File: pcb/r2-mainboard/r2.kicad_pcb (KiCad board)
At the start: 4 copper layers, 185.5 x 95 mm, 327 parts, among them J1 USB-C 16P, J2 Pico-Lock 504050-0391, J20 SWD+JTAG (DNP), J21 MICRO_SD(TFC-WPAPR-08), J22 HC-FPC-05-09-6RLTAG, J23 HC-FPC-05-09-6RLTAG, J24 HC-FPC-05-09-8RLTAG, J25 SolderPads 3x, J26 BTH-060-01-L-D-A-K-TR, J27 BTH-060-01-L-D-A-K-TR, J6 FPC-05F-50PH20, Q1 AO3401A, Q2 S8050, Q6 AO3400A, Q7 AO3401A, Q8 AO3401A, Q9 AO3400A, SW20 SW, SW21 SW, SW22 SW, U1 BQ25892RTW, U10 TPS7A0233DBVR, U12 TPS61022RWUR, U13 TPS63802DLAR, U14 TPS62A02DRLR, U15 TPS62A02DRLR, U2 MAX17048G+T10, U20 STM32G0B1RCT6, U21 INA3221, U22 INA3221, U23 LGS6302B5, U24 LGS6302B5, U26 LGS5145, U27 INA3221, U3 USBLC6-2SC6, U31 LM321, U41 XC6SLX-FTG256, U42 W25Q128JVSIQ, U52 MT41K64M16TW, U53 LM3630A, U54 TPS22914BYFPR, U55 TPS22914BYFPR, U6 MT9700, U7 TPS22914BYFPR, U8 TPS22914BYFPR, U9 LGS5145, X1 33.33MHz, X2 PCM-071, Y20 32.768kHz

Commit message: R2: settings applied, and 200 of the board's 244 DRC errors were mine
The owner ran tools/import_r1_settings.py --write. check_pcb.py now reports
8 of 8 net classes present, 122 nets assigned, 0 dead patterns.

Their own KiCad "import settings from another project" had already pulled R1's
constraints and presets across first, which is visible in the script's before
column -- and shows exactly why that is not enough on its own: it brought R1's
class NAMES (DP, LVDS, SDRAM_A/H/L, POWER) and R1's patterns, none of which
match an R2 net. Every net would have routed on Default.

Then the DRC that followed found 244 violations, 200 of them solder_mask_bridge
on J26 and J27 -- footprints this repo generates. They are not a mistake:
MASK_MARGIN 0.102 on a 0.5 mm pitch makes each aperture 0.509, so a row is one
gang opening, which is what Samtec's own footprint does and what the pitch
requires (the 0.093 web the alternative needs is under JLCPCB's 0.1 minimum and
would be dropped anyway, silently). What was missing is the attribute that tells
KiCad so. Both footprints, the generator, and the two placed instances now carry
`allow_soldermask_bridges`. Board total: 244 -> 44, and the 44 left are silk and
edge-clearance noise that placement will clear.

Samtec's file lacks the attribute only because it is a tedit-era KiCad 5/6
footprint that predates it.

Two things learned, both recorded:

- `kicad-cli pcb drc` SILENTLY IGNORES a .kicad_dru it cannot parse. No error,
  no warning, exit 0, rules just not applied -- verified by feeding it a
  deliberately unterminated rule and getting identical clean output. So the
  clean run on r2.kicad_dru proves nothing about its validity; only Board Setup
  > Custom Rules > "Check rule syntax" does. layout.md §9.2, and the script now
  says so on exit.

- Patching footprints in a loop over re.finditer while mutating the text skips
  every match after the first, because the offsets shift. J26 was silently left
  unpatched and only surfaced as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
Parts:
- moved C1 10.5 mm to (57.0, 37.0)
- moved C2 10.4 mm to (61.0, 35.5), turned to 180 degrees
- moved L1 2.60 mm to (68.0, 36.0)
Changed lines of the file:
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@@
 		(35 "F.Fab" user)
 		(33 "B.Fab" user)
-		(39 "User.1" user)
-		(41 "User.2" user)
-		(43 "User.3" user)
-		(45 "User.4" user)
 	)
 	(setup
@@
 		(capping no)
 		(filling no)
+		(zone_defaults)
 		(pcbplotparams
 			(layerselection 0x00000000_00000000_55555555_5755f5ff)
@@
 			)
 		)
-		(attr smd)
+		(attr smd allow_soldermask_bridges)
 		(duplicate_pad_numbers_are_jumpers no)
 		(fp_line
@@
 	(footprint "Capacitor_SMD:C_0402_1005Metric"
 		(layer "F.Cu")
-		(at 50.81 45.53)
+		(at 57 37)
 		(descr "Capacitor SMD 0402 (1005 Metric), square (rectangular) end terminal, IPC-7351 nominal, (Body size source: IPC-SM-782 page 76, https://www.pcb-3d.com/wordpress/wp-content/uploads/ipc-sm-782a_amendment_1_and_2.pdf)")
 		(tags "capacitor")
@@
 	(footprint "Inductor_SMD:L_Taiyo-Yuden_NR-30xx"
 		(layer "F.Cu")
-		(at 65.6 37)
+		(at 68 36)
 		(descr "Inductor, Taiyo Yuden, NR series, Taiyo-Yuden_NR-30xx, 3.0mmx3.0mm")
 		(tags "inductor taiyo-yuden nr smd")
@@
 			)
 		)
-		(attr smd)
+		(attr smd allow_soldermask_bridges)
 		(duplicate_pad_numbers_are_jumpers no)
 		(fp_line
@@
 	(footprint "Capacitor_SMD:C_0805_2012Metric"
 		(layer "F.Cu")
-		(at 51.6 31)
+		(at 61 35.5 180)
 		(descr "Capacitor SMD 0805 (2012 Metric), square (rectangular) end terminal, IPC-7351 nominal, (Body size source: IPC-SM-782 page 76, https://www.pcb-3d.com/wordpress/wp-content/uploads/ipc-sm-782a_amendment_1_and_2.pdf, https://docs.google.com/spreadsheets/d/1BsfQQcO9C6DZCsRaXUlFlo91Tg2WpOkGARC1WS5S8t0/edit?usp=sharing)")
 		(tags "capacitor")
 		(property "Reference" "C2"
-			(at 0 -1.68 0)
+			(at -2.5 3 0)
 			(layer "F.SilkS")
 			(effects
@@
 		(duplicate_pad_numbers_are_jumpers no)
 		(fp_line
-			(start -0.261252 -0.735)
-			(end 0.261252 -0.735)
+			(start -0.261252 0.735)
+			(end 0.261252 0.735)
 			(stroke
 				(width 0.12)
@@
 		)
 		(fp_line
-			(start -0.261252 0.735)
-			(end 0.261252 0.735)
+			(start -0.261252 -0.735)
+			(end 0.261252 -0.735)
 			(stroke
 				(width 0.12)
@@
 		)
 		(fp_text user "${REFERENCE}"
-			(at 0 0 0)
+			(at 0 0 180)
 			(unlocked yes)
 			(layer "F.Fab")
@@
 		)
 		(pad "1" smd roundrect
-			(at -0.95 0)
+			(at -0.95 0 180)
 			(size 1 1.45)
 			(layers "F.Cu" "F.Mask" "F.Paste")
@@
 		)
 		(pad "2" smd roundrect
-			(at 0.95 0)
+			(at 0.95 0 180)
 			(size 1 1.45)
 			(layers "F.Cu" "F.Mask" "F.Paste")
@@
 		(tags "WQFN NoLead")
 		(property "Reference" "U1"
-			(at 0 -3.33 0)
+			(at 4.05 -1.85 0)
 			(layer "F.SilkS")
 			(effects
@@
 		(layer "Edge.Cuts")
 	)
+	(segment
+		(start 60.45 39.35)
+		(end 60.5 39.3)
+		(width 0.1)
+		(layer "F.Cu")
+		(net "GND")
+	)
+	(segment
+		(start 60.5 39.3)
+		(end 60.5 39)
+		(width 0.1)
+		(layer "F.Cu")
+		(net "GND")
+	)
 	(group "SoM: X2 + J26 + J27"

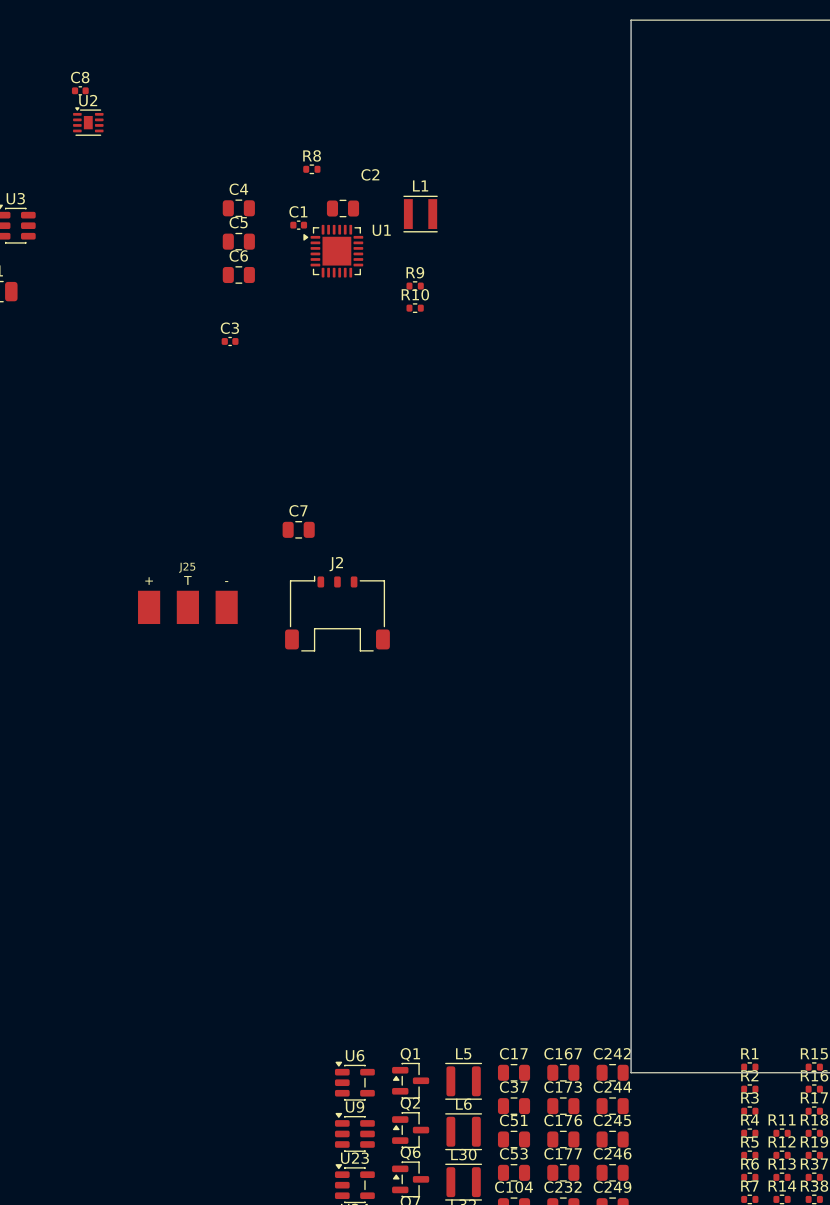
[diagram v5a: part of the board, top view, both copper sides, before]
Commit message: R2: C6 goes 0805/10V -> 0603/16V, and clears two DRC errors doing it
The question was whether the REGN decoupling cap could be smaller. It can,
and the smaller part is the better part -- but not for the reason the doc
gave.

bq25896.pdf pin 22 asks for "a 4.7 uF (10 V rating) ceramic capacitor",
placed close to the IC, and gives no range around it -- unlike tps63802.pdf
which publishes a 10-50 uF window for its output cap. So the value is fixed
and the package is the only free variable. REGN sits at 4.7-4.8 V here (spec
table, V(VBUS) = 5 V), and a ceramic loses capacitance with the field across
its dielectric, so a higher rating in a smaller case can beat a lower rating
in a larger one.

Fitted: LCSC C19666, Samsung CL10A475KO8NNNC, 4.7 uF 16 V X5R 0603, a JLCPCB
basic part with 6.35 M in stock. It keeps TI's value, exceeds TI's rating,
and is smaller and lower-ESL than the 0805 -- which serves bq25896.pdf
section 12.1 guideline 6 better than the part it replaces. 0402 was rejected:
the cheap one is +-20 % before derating at 2.1x voltage margin, and the 25 V
one costs 4x a basic part to save 0.7 mm2.

DRC went 46 -> 44. The 0805's pad 2 sat 0.075 mm from a Net-(C3-Pad2) track
against the PWR netclass's 0.110 mm; 0603 pulls it back 0.175 mm and clears
both violations. Unconnected unchanged at 499, ERC unchanged at 32.

battery.md section 6 is corrected while here. It claimed the TS divider's
loading is why 4.7 uF is not optional. It is not -- that divider draws 377 uA
of steady DC, which constrains the LDO, not the capacitor. The reasons are
pin 22 and the gate drive. Ripple was checked and is not binding either: even
at a generous 20 nC per cycle, 1 uF effective gives 0.42 % of REGN against
1-1.4 % TS hysteresis bands.

C6 also gained the check_pcb.py proximity rule it never had, 5.0 mm to U1,
the same limit as its neighbours C1/C2/C3. It sits at 4.15 mm and passes.

Note: r2.kicad_pcb and r2.kicad_pro in this commit also carry the owner's
uncommitted placement wor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
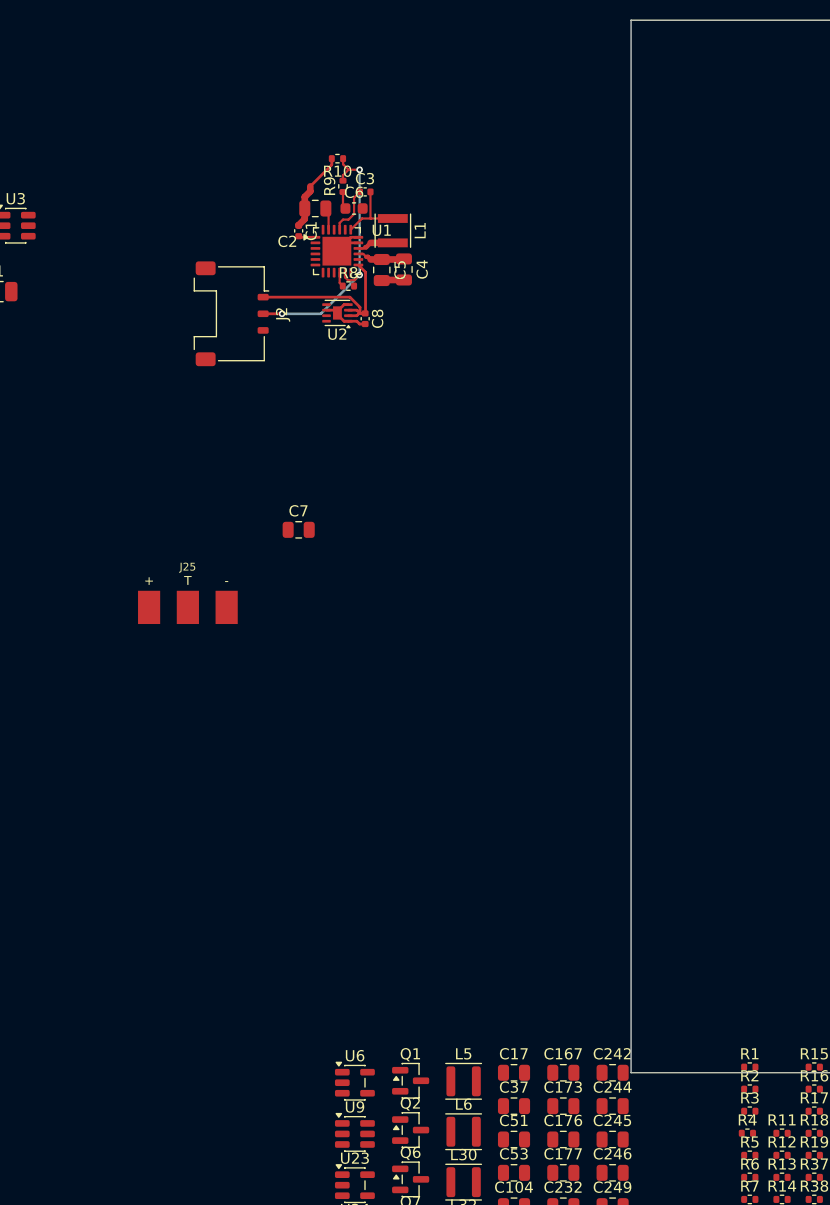
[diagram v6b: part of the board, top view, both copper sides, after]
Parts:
- C6: value 4.7uF/10V -> 4.7uF/16V; footprint Capacitor_SMD:C_0805_2012Metric -> Capacitor_SMD:C_0603_1608Metric
- moved C8 32.9 mm to (63.0, 45.4), turned to -90 degrees
- moved J2 28.6 mm to (51.0, 45.0), turned to -90 degrees
- moved U2 28.3 mm to (60.5, 44.9), turned to 180 degrees
- moved C3 18.2 mm to (63.0, 34.0)
- moved C4 15.9 mm to (66.5, 41.0), turned to -90 degrees
- moved R10 15.2 mm to (60.5, 31.0), turned to 180 degrees
- moved C5 13.2 mm to (64.5, 41.0), turned to -90 degrees
- moved C6 12.0 mm to (62.0, 35.5)
- moved R9 11.1 mm to (61.0, 33.5), turned to 90 degrees
- moved R8 11.0 mm to (61.5, 42.5)
- moved L1 2.92 mm to (65.5, 37.5), turned to -90 degrees
- moved C2 2.50 mm to (58.5, 35.5), turned to 0 degrees
- moved C1 0.52 mm to (57.0, 37.5), turned to -90 degrees
- moved R4 0.22 mm to (97.5, 119.0)
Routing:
- net /battery/CHG_TS: track 0.00 -> 25.1 mm, vias 0 -> 3
- net GND: track 0.37 -> 19.9 mm
- net +VBAT: track 0.00 -> 17.5 mm
- net +VSYS: track 0.00 -> 7.16 mm
- net Net-(C3-Pad2): track 0.00 -> 6.15 mm
- net Net-(U1-BTST): track 0.00 -> 4.46 mm
- net /battery/REGN: track 0.00 -> 1.67 mm
- net Net-(U1-PMID): track 0.00 -> 1.56 mm
- net +VBUS: track 0.00 -> 1.55 mm
- net Net-(U1-ILIM): track 0.00 -> 1.33 mm
- added copper zone on In1.Cu, net GND

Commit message: R2: withdraw the RWU0007A thermal-pad concern -- it was wrong
power.md §7 item 2 said KiCad's Texas_RWU0007A_VQFN-7_2x2mm_P0.5mm leaves the
thermal-pad segments unnumbered, so U12's heat path is not tied to GND, and to
copy the footprint into r2.pretty and renumber those pads 1 before layout.

Reading the placed footprint with the layer field visible: the six unnumbered
pads are F.Paste ONLY. They are stencil apertures -- each large pad split into
two openings to control solder volume, the standard idiom at that size. Pads
1/2/3 are F.Cu + F.Mask, numbered, and netted GND / SW / +5V_DCDC. Pin 1 is the
thermal path per Table 5-1 and it is on GND already.

Acting on the note would have renumbered paste apertures into copper and
shorted GND, SW and VOUT together -- creating the failure it was meant to
prevent. Found because the owner is routing U12 right now.

§11.2 item 5 amended to a plain layout instruction, and §8's open-items list
no longer carries it.

Co-Authored-By: Claude Opus 5 <noreply@anthropic.com>
Claude-Session: https://claude.ai/code/session_01MnesETWABbVdbcVnCKfKVs
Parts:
- removed R14, R15: 0R, Resistor_SMD:R_0402_1005Metric
- removed R16: 10k, Resistor_SMD:R_0402_1005Metric
- C4, C5, C7: footprint Capacitor_SMD:C_0805_2012Metric -> Capacitor_SMD:C_0402_1005Metric
- moved U13 139.9 mm to (75.4, 49.2)
- moved U15 127.8 mm to (77.7, 32.8)
- moved L13 126.0 mm to (77.1, 27.4)
- moved C34 125.1 mm to (83.2, 29.6)
- moved U12 123.8 mm to (101.2, 35.4)
- moved R36 122.1 mm to (81.8, 31.2)
- moved C33 121.8 mm to (76.7, 30.9)
- moved R35 120.7 mm to (79.5, 31.3)
- moved R33 120.1 mm to (80.5, 27.7)
- moved R34 120.1 mm to (80.5, 29.6)
- moved C28 120.0 mm to (101.5, 37.4)
- moved R23 119.7 mm to (101.3, 27.6)
- moved C21 118.8 mm to (79.8, 40.4), turned to -90 degrees
- moved C20 118.5 mm to (74.6, 40.4), turned to -90 degrees
- moved U10 117.2 mm to (77.2, 40.9)
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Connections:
- net /USB_DM renamed /USBD-
- net /USB_DP renamed /USBD+
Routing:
- net +VBAT: track 17.5 -> 55.8 mm
- net /battery/CHG_TS: track 25.1 -> 3.40 mm, vias 3 -> 1
- net Net-(F1-Pad1): track 0.00 -> 7.73 mm, vias 0 -> 2
- net /battery/USB_CC1: track 0.00 -> 7.44 mm
- net /battery/USB_CC2: track 0.00 -> 5.70 mm
- net Net-(J1-D--PadA7): track 0.00 -> 5.16 mm
- net Net-(J1-D+-PadA6): track 0.00 -> 5.12 mm
- net +VSYS: track 7.16 -> 10.2 mm
- net +VBUS: track 1.55 -> 3.32 mm
- net +3V3_AON_DCDC: track 0.00 -> 1.74 mm
- net GND: track 19.9 -> 19.0 mm, vias 0 -> 2
- added copper zone on F.Cu, net GND
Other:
- board size 185.5 x 95 mm -> 245.3 x 165.7 mm

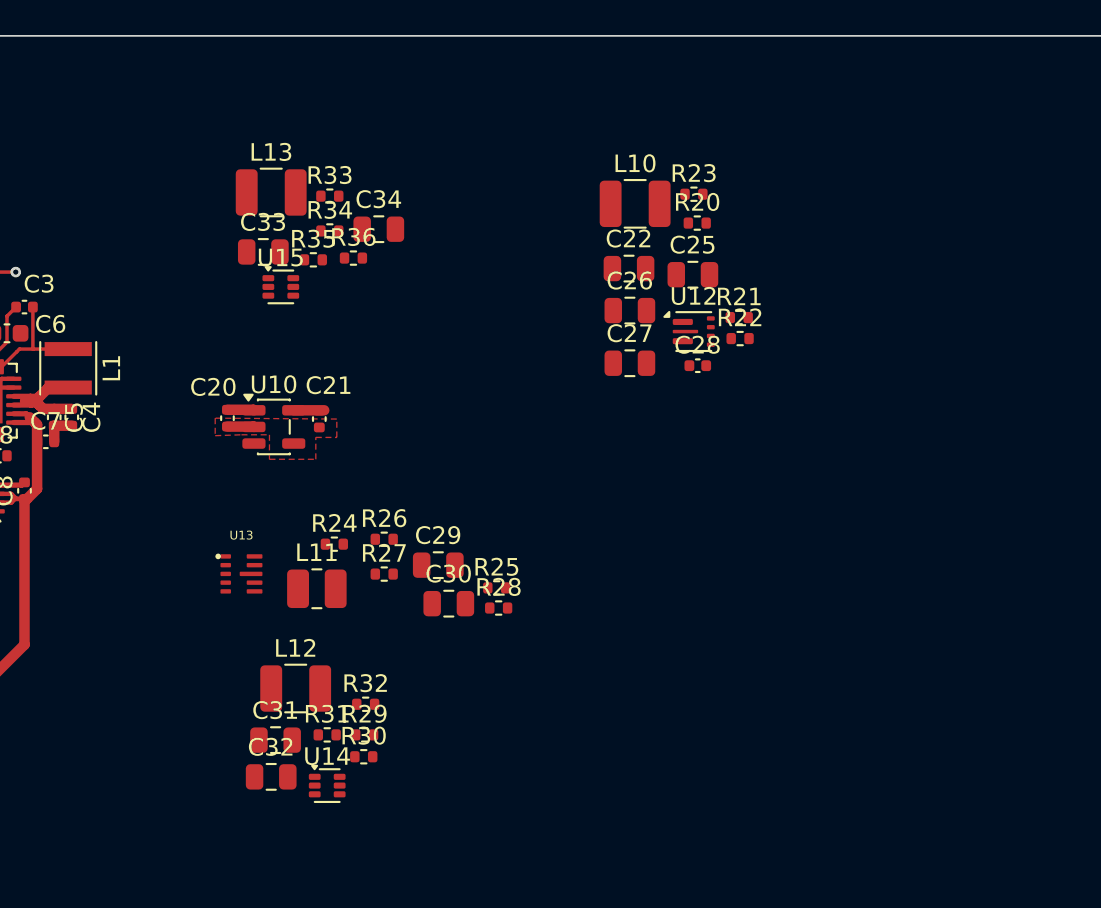
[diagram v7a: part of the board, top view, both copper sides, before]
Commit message: R2: GND does not belong in a width class, and a check that says why
The owner, mid-route: "I can't always have a 0.6 mm GND trace. Sometimes for
signals it's just not necessary." Correct, and the class was at fault.

GND was in PWR, whose track width is 0.6 mm. But GND's current path is the
In1.Cu plane; a GND segment is almost always a short stub from a pad to a
stitching via, where 0.6 mm buys nothing and gets overridden by hand every
time. On Default it routes at 0.2 mm and takes a 0.6/0.3 via, which is also the
more useful stitching via -- PWR's 0.8/0.35 is clumsy under a BGA. Clearance is
0.11 either way. +VSYS stays in PWR: unlike GND it has real routed runs to the
four converters that should start wide.

The first idea for a check was "every segment must meet its net class width".
GND is exactly why that is wrong: it would have flagged dozens of correct 0.2 mm
stubs, and a noisy check gets switched off, taking the real findings with it. So
check 7 is inverted -- only nets where a document states a current, each entry
carrying that current and its source, with the width from IPC-2152 at 1 oz and
20 C rise rounded DOWN to a floor. A net absent from the table is not unimportant;
it is a net nobody has put a number on yet.

It finds 8 of the 10 listed nets routed and all 8 too thin, the worst being
Net-(U12-SW) at 0.13 mm on a node carrying ~2.8 A average and 3.4 A peak.

Also fixes a trap in import_r1_settings.py: it assigned the class list wholesale,
so a second run would have silently deleted the owner's hand-made Signals_NET
class. It now keeps any class it did not create, and their patterns with them.

Co-Authored-By: Claude Opus 5 <noreply@anthropic.com>
Claude-Session: https://claude.ai/code/session_01MnesETWABbVdbcVnCKfKVs
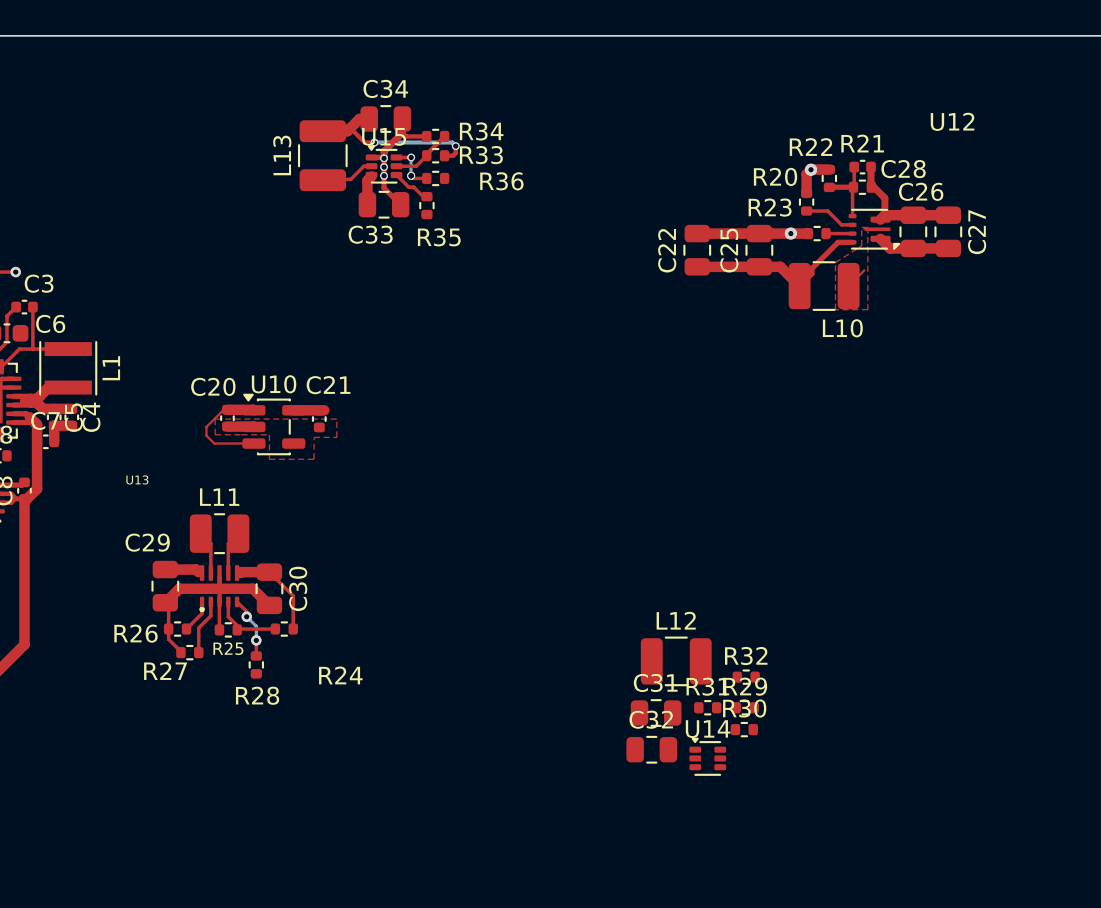
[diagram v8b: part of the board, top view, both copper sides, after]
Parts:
- moved C32 21.8 mm to (98.8, 59.3)
- moved R29 21.8 mm to (104.2, 56.9)
- moved R30 21.8 mm to (104.1, 58.1)
- moved R31 21.8 mm to (102.0, 56.9)
- moved R32 21.8 mm to (104.2, 55.1)
- moved C31 21.8 mm to (99.1, 57.2)
- moved L12 21.8 mm to (100.2, 54.2)
- moved U14 21.8 mm to (102.0, 59.8)
- moved C27 19.7 mm to (115.8, 29.7), turned to -90 degrees
- moved C26 16.8 mm to (113.8, 29.7), turned to -90 degrees
- moved C29 15.6 mm to (71.0, 50.0), turned to -90 degrees
- moved R25 15.5 mm to (74.7, 52.5), turned to 180 degrees
- moved C28 14.7 mm to (110.9, 26.0), turned to 180 degrees
- moved R28 14.2 mm to (76.2, 54.5), turned to 90 degrees
- moved R26 12.9 mm to (71.8, 52.4), turned to 180 degrees
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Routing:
- net GND: track 19.0 -> 53.3 mm, vias 2 -> 7
- net +VSYS: track 10.2 -> 31.3 mm
- net +1V5_DCDC: track 0.00 -> 10.5 mm, vias 0 -> 2
- net +5V_DCDC: track 0.00 -> 7.15 mm
- net +3V3_DCDC: track 0.00 -> 5.48 mm
- net Net-(U12-FB): track 0.00 -> 4.26 mm
- net Net-(U13-FB): track 0.00 -> 3.83 mm
- net /PG_3V3: track 0.00 -> 3.55 mm, vias 0 -> 2
- net Net-(U15-FB): track 0.00 -> 3.50 mm
- net Net-(U13-MODE): track 0.00 -> 3.19 mm
- net /MCU_EN_5V: track 0.00 -> 2.95 mm
- net Net-(U15-SW): track 0.00 -> 2.85 mm
- net /PG_1V5: track 0.00 -> 2.84 mm, vias 0 -> 3
- net Net-(U13-L1): track 0.00 -> 2.49 mm
- net Net-(U13-L2): track 0.00 -> 2.49 mm
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- added copper zone on F.Cu, net Net-(U12-SW)
